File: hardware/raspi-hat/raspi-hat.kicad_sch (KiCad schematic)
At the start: 7 parts, among them J1 ATX-20, J2 Raspberry_Pi_4, U1 STSPIN32G4, Y1 Crystal_GND23_Small

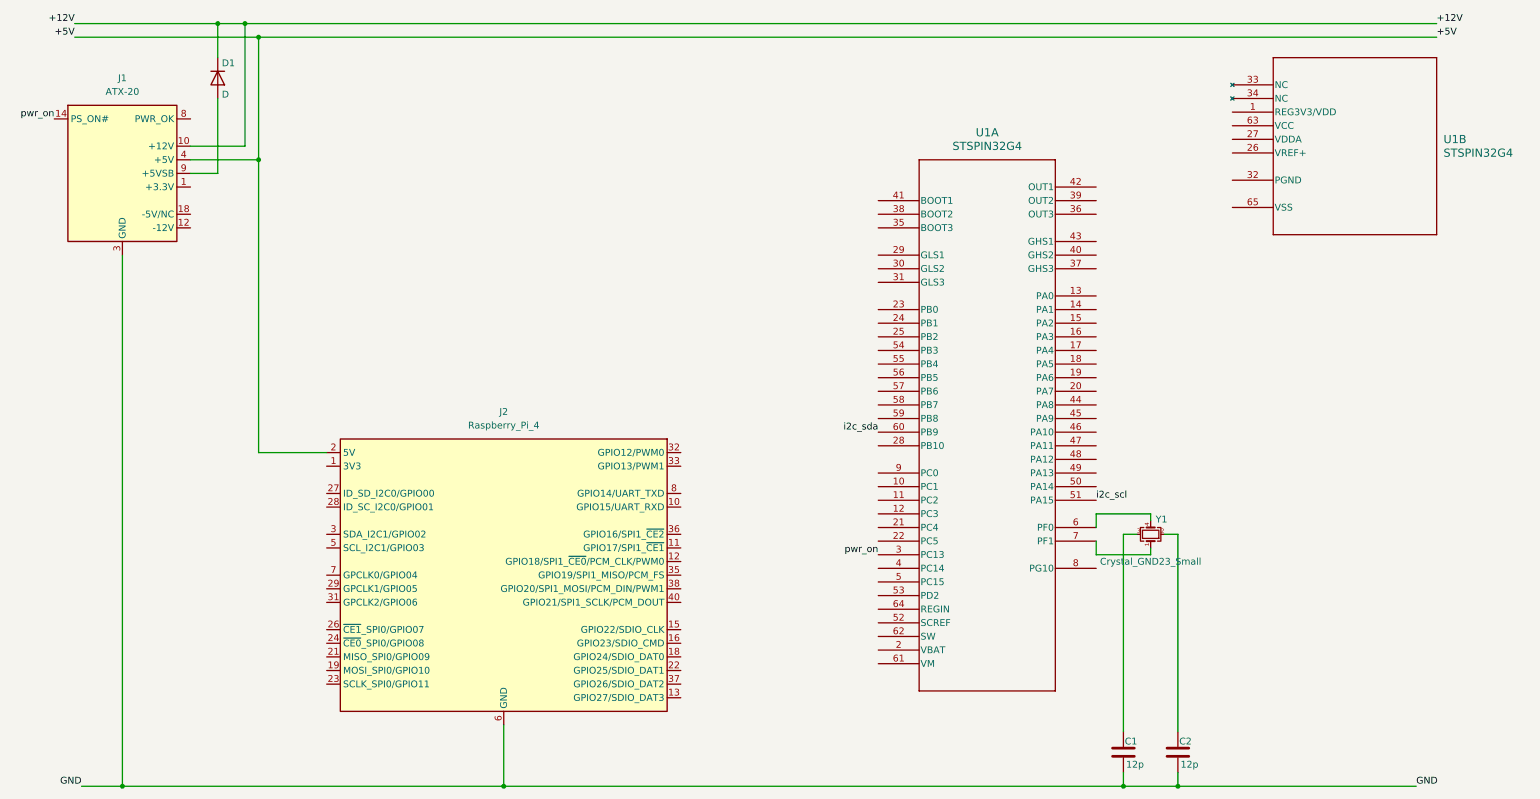
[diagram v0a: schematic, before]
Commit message: updated symbol of stsping4
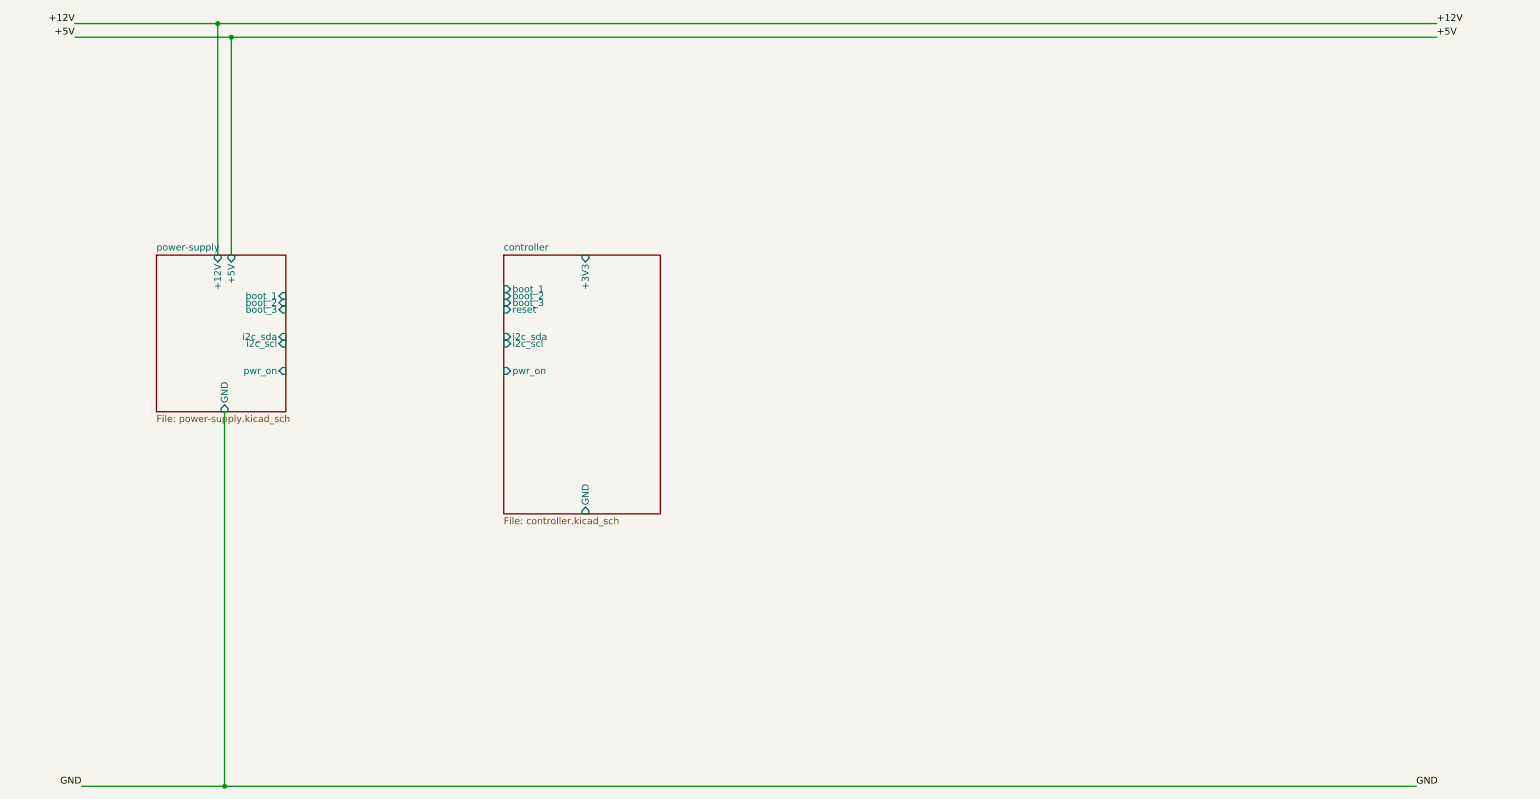
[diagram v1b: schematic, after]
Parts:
- removed C1, C2: 12p, Capacitor_SMD:C_0603_1608Metric, symbol Device:C
- removed D1: D, symbol Device:D
- removed J1: ATX-20, Connector_Molex:Molex_Mini-Fit_Jr_5569-20A2_2x10_P4.20mm_Horizontal, symbol Connector:ATX-20
- removed J2: Raspberry_Pi_4, symbol Connector:Raspberry_Pi_4
- removed U1: STSPIN32G4, QFN_IN32G4_STM, symbol stsping4:STSPIN32G4
- removed Y1: Crystal_GND23_Small, Crystal:Crystal_SMD_0603-4Pin_6.0x3.5mm, symbol Device:Crystal_GND23_Small
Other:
- added sheet controller (controller.kicad_sch)
- added sheet power-supply (power-supply.kicad_sch)

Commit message: - added some lines on hardwaer - added libmotor as dependency
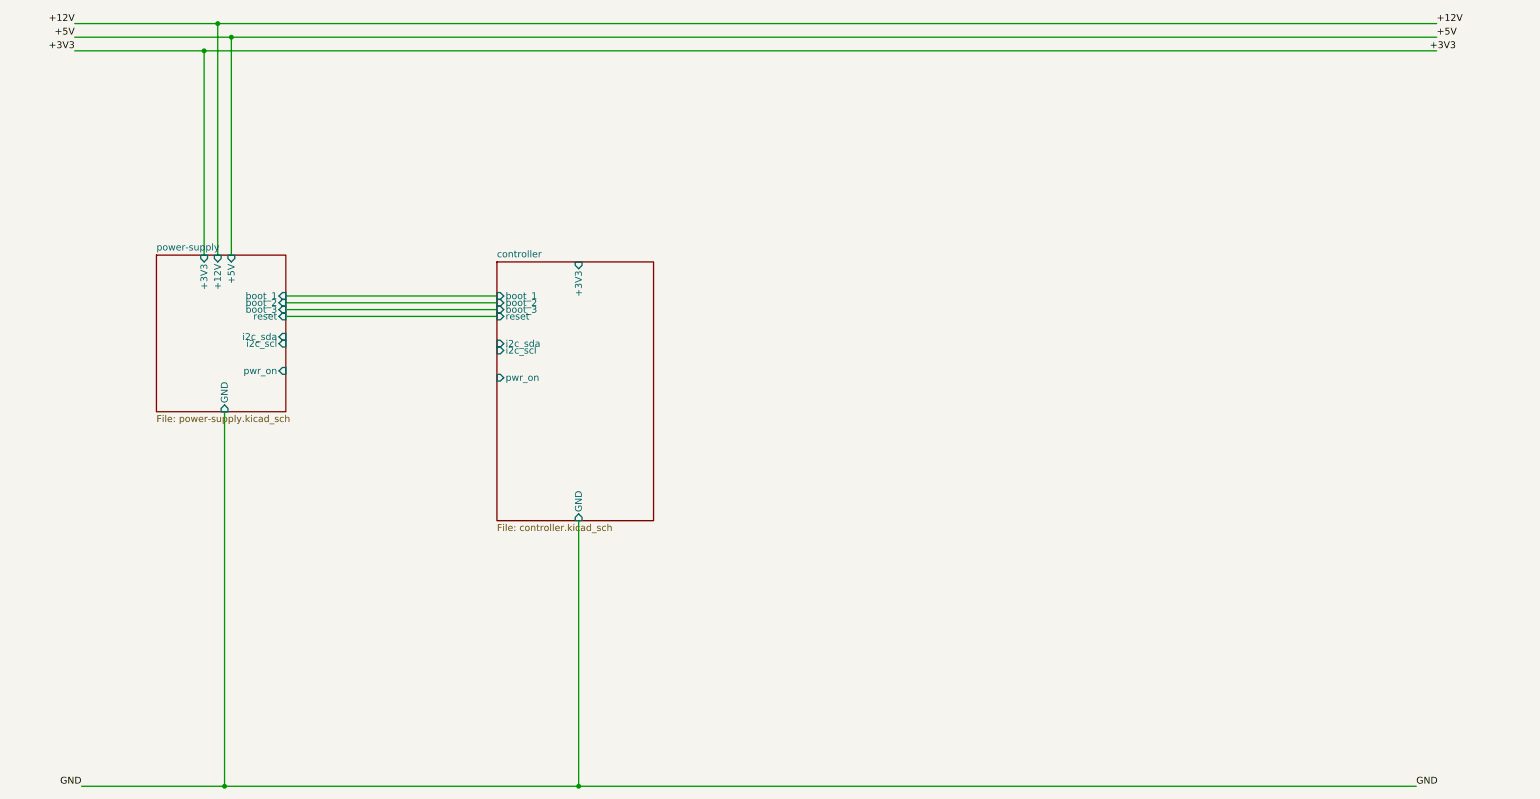
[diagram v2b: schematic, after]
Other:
- sheet power-supply ports: added +3V3, reset; removed none
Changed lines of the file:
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@@
+	)
+	(junction
+		(at 46.99 24.13)
+		(diameter 0)
+		(color 0 0 0 0)
 	)
 	(junction
@@
 		(color 0 0 0 0)
 	)
+	(junction
+		(at 116.84 161.29)
+		(diameter 0)
+		(color 0 0 0 0)
+	)
 	(wire
 		(pts
@@
 	(wire
 		(pts
+			(xy 46.99 62.23) (xy 46.99 24.13)
+		)
+		(stroke
+			(width 0)
+			(type default)
+		)
+	)
+	(wire
+		(pts
+			(xy 22.86 24.13) (xy 46.99 24.13)
+		)
+		(stroke
+			(width 0)
+			(type default)
+		)
+	)
+	(wire
+		(pts
 			(xy 22.86 19.05) (xy 49.53 19.05)
 		)
@@
 	(wire
 		(pts
+			(xy 62.23 71.12) (xy 101.6 71.12)
+		)
+		(stroke
+			(width 0)
+			(type default)
+		)
+	)
+	(wire
+		(pts
+			(xy 116.84 111.76) (xy 116.84 161.29)
+		)
+		(stroke
+			(width 0)
+			(type default)
+		)
+	)
+	(wire
+		(pts
 			(xy 52.07 21.59) (xy 52.07 62.23)
 		)
@@
 	(wire
 		(pts
+			(xy 46.99 24.13) (xy 276.86 24.13)
+		)
+		(stroke
+			(width 0)
+			(type default)
+		)
+	)
+	(wire
+		(pts
 			(xy 50.8 91.44) (xy 50.8 161.29)
 		)
@@
 	(wire
 		(pts
+			(xy 116.84 161.29) (xy 273.05 161.29)
+		)
+		(stroke
+			(width 0)
+			(type default)
+		)
+	)
+	(wire
+		(pts
 			(xy 52.07 21.59) (xy 276.86 21.59)
 		)
@@
 	(wire
 		(pts
-			(xy 50.8 161.29) (xy 273.05 161.29)
+			(xy 62.23 73.66) (xy 101.6 73.66)
+		)
+		(stroke
+			(width 0)
+			(type default)
+		)
+	)
+	(wire
+		(pts
+			(xy 62.23 72.39) (xy 101.6 72.39)
+		)
+		(stroke
+			(width 0)
+			(type default)
+		)
+	)
+	(wire
+		(pts
+			(xy 50.8 161.29) (xy 116.84 161.29)
 		)
 		(stroke
@@
 		(pts
 			(xy 22.86 21.59) (xy 52.07 21.59)
+		)
+		(stroke
+			(width 0)
+			(type default)
+		)
+	)
+	(wire
+		(pts
+			(xy 62.23 69.85) (xy 101.6 69.85)
 		)
 		(stroke
@@
 		)
 	)
+	(label "+3V3"
+		(at 275.59 24.13 0)
+		(effects
+			(font
+				(size 1.27 1.27)
+			)
+			(justify left bottom)
+		)
+	)
 	(label "+12V"
 		(at 276.86 19.05 0)
@@
 	(label "GND"
 		(at 24.13 161.29 180)
+		(effects
+			(font
+				(size 1.27 1.27)
+			)
+			(justify right bottom)
+		)
+	)
+	(label "+3V3"
+		(at 22.86 24.13 180)
 		(effects
 			(font
@@
 			)
 		)
+		(pin "reset" input
+			(at 62.23 73.66 0)
+			(effects
+				(font
+					(size 1.27 1.27)
+				)
+				(justify right)
+			)
+		)
+		(pin "+3V3" input
+			(at 46.99 62.23 90)
+			(effects
+				(font
+					(size 1.27 1.27)
+				)
+				(justify right)
+			)
+		)
 		(instances
 			(project "raspi-hat"
@@
 	)
 	(sheet
-		(at 102.87 62.23)
+		(at 101.6 63.5)
 		(size 29.21 48.26)
 		(exclude_from_sim no)
@@
 		)
 		(property "Sheetname" "controller"
-			(at 102.87 61.5184 0)
+			(at 101.6 62.7884 0)
 			(effects
 				(font
@@
 		)
 		(property "Sheetfile" "controller.kicad_sch"
-			(at 102.87 111.0746 0)
+			(at 101.6 112.3446 0)
 			(effects
 				(font
@@
 		)
 		(pin "+3V3" input
-			(at 118.11 62.23 90)
+			(at 116.84 63.5 90)
 			(effects
 				(font
@@
 		)
 		(pin "boot_1" input
-			(at 102.87 68.58 180)
+			(at 101.6 69.85 180)
 			(effects
 				(font
@@
 		)
 		(pin "boot_2" input
-			(at 102.87 69.85 180)
+			(at 101.6 71.12 180)
 			(effects
 				(font
@@
 		)
 		(pin "boot_3" input
-			(at 102.87 71.12 180)
+			(at 101.6 72.39 180)
 			(effects
 				(font
@@
 		)
 		(pin "GND" input
-			(at 118.11 110.49 270)
+			(at 116.84 111.76 270)
 			(effects
 				(font
@@
 		)
 		(pin "i2c_scl" input
-			(at 102.87 78.74 180)
+			(at 101.6 80.01 180)
 			(effects
 				(font
@@
 		)
 		(pin "i2c_sda" input
-			(at 102.87 77.47 180)
+			(at 101.6 78.74 180)
 			(effects
 				(font
@@
 		)
 		(pin "pwr_on" input
-			(at 102.87 83.82 180)
+			(at 101.6 85.09 180)
 			(effects
 				(font
@@
 		)
 		(pin "reset" input
-			(at 102.87 72.39 180)
-			(effects
-				(font
+			(at 101.6 73.66 180)
+			(effects
+				(font

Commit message: updatd ioc
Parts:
- added J2: Conn_01x03_Pin, symbol Connector:Conn_01x03_Pin
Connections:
- new net controller/phase_u: J2.1 (Pin_1)
- new net controller/phase_v: J2.2 (Pin_2)
- new net controller/phase_w: J2.3 (Pin_3)
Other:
- sheet controller ports: added +12V, boot, phase_u, phase_v, phase_w, uart_rx, uart_tx; removed boot_1, boot_2, boot_3, i2c_scl, i2c_sda, pwr_on
- sheet power-supply ports: added boot, uart_rx, uart_tx; removed boot_1, boot_2, boot_3

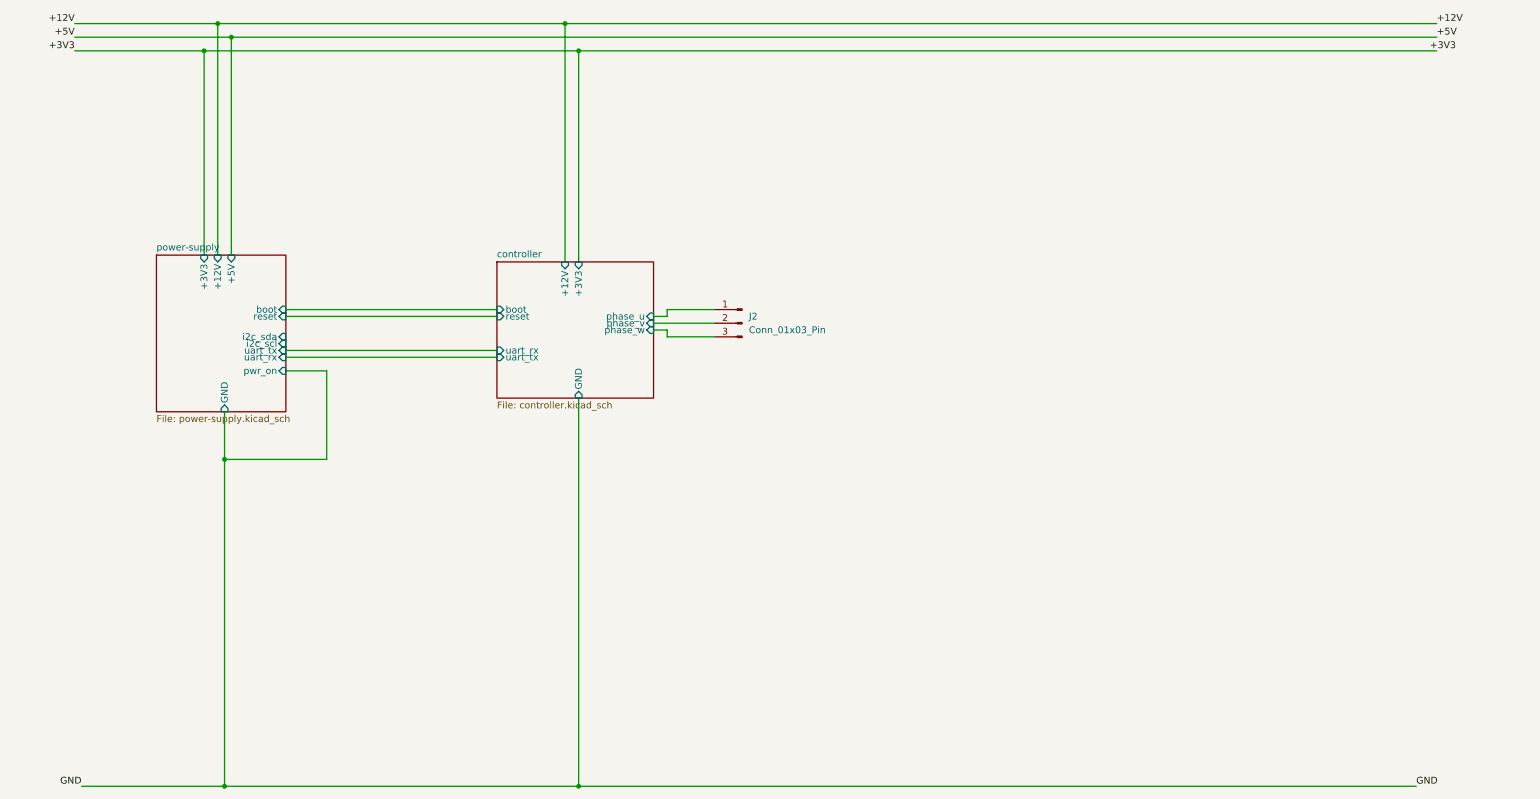
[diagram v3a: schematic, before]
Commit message: added more parts
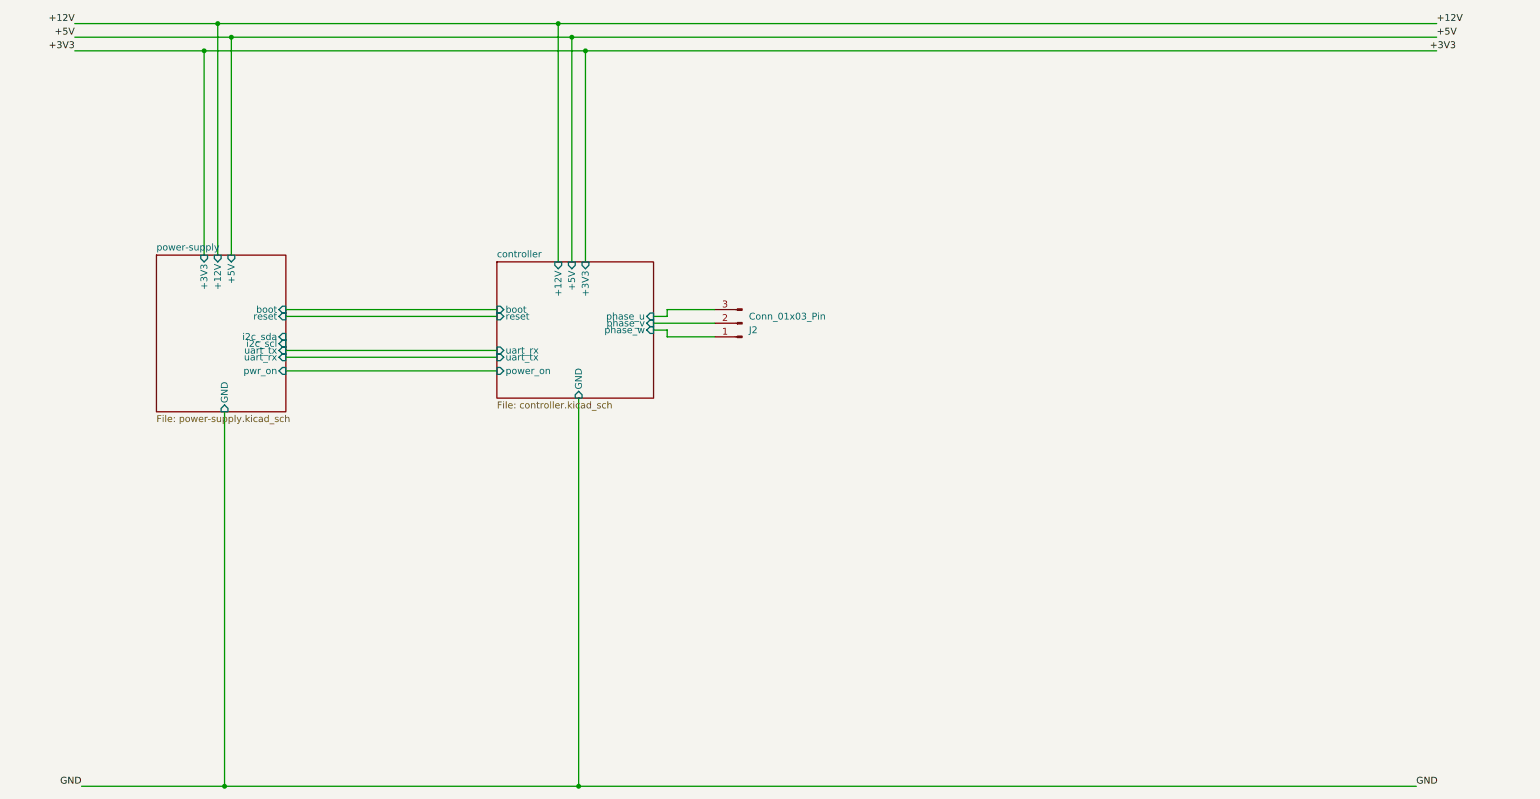
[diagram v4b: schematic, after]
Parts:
- J2: footprint (none) -> Connector_Phoenix_MSTB:PhoenixContact_MSTBA_2,5_3-G_1x03_P5.00mm_Horizontal
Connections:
- net controller/phase_u: now also J2.3 (Pin_3); no longer J2.1 (Pin_1)
- net controller/phase_w: now also J2.1 (Pin_1); no longer J2.3 (Pin_3)
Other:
- sheet controller ports: added +5V, power_on; removed none
- moved on the sheet: J2
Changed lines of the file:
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@@
-	)
-	(junction
-		(at 50.8 100.33)
-		(diameter 0)
-		(color 0 0 0 0)
-	)
-	(junction
-		(at 116.84 24.13)
-		(diameter 0)
-		(color 0 0 0 0)
 	)
 	(junction
@@
 	)
 	(junction
-		(at 114.3 19.05)
+		(at 118.11 24.13)
+		(diameter 0)
+		(color 0 0 0 0)
+	)
+	(junction
+		(at 113.03 19.05)
 		(diameter 0)
 		(color 0 0 0 0)
@@
 		(color 0 0 0 0)
 	)
+	(junction
+		(at 115.57 21.59)
+		(diameter 0)
+		(color 0 0 0 0)
+	)
+	(wire
+		(pts
+			(xy 113.03 19.05) (xy 276.86 19.05)
+		)
+		(stroke
+			(width 0)
+			(type default)
+		)
+	)
 	(wire
 		(pts
@@
 	(wire
 		(pts
-			(xy 116.84 24.13) (xy 276.86 24.13)
-		)
-		(stroke
-			(width 0)
-			(type default)
-		)
-	)
-	(wire
-		(pts
 			(xy 52.07 21.59) (xy 52.07 62.23)
 		)
@@
 	(wire
 		(pts
-			(xy 114.3 19.05) (xy 276.86 19.05)
-		)
-		(stroke
-			(width 0)
-			(type default)
-		)
-	)
-	(wire
-		(pts
-			(xy 46.99 24.13) (xy 116.84 24.13)
+			(xy 115.57 21.59) (xy 276.86 21.59)
+		)
+		(stroke
+			(width 0)
+			(type default)
+		)
+	)
+	(wire
+		(pts
+			(xy 46.99 24.13) (xy 118.11 24.13)
 		)
 		(stroke
@@
 	(wire
 		(pts
-			(xy 116.84 24.13) (xy 116.84 63.5)
+			(xy 118.11 24.13) (xy 118.11 63.5)
 		)
 		(stroke
@@
 	(wire
 		(pts
-			(xy 69.85 83.82) (xy 69.85 100.33)
-		)
-		(stroke
-			(width 0)
-			(type default)
-		)
-	)
-	(wire
-		(pts
-			(xy 50.8 91.44) (xy 50.8 100.33)
-		)
-		(stroke
-			(width 0)
-			(type default)
-		)
-	)
-	(wire
-		(pts
-			(xy 69.85 100.33) (xy 50.8 100.33)
+			(xy 50.8 91.44) (xy 50.8 161.29)
 		)
 		(stroke
@@
 	(wire
 		(pts
-			(xy 52.07 21.59) (xy 276.86 21.59)
+			(xy 52.07 21.59) (xy 115.57 21.59)
 		)
 		(stroke
@@
 	(wire
 		(pts
-			(xy 49.53 19.05) (xy 114.3 19.05)
+			(xy 49.53 19.05) (xy 113.03 19.05)
+		)
+		(stroke
+			(width 0)
+			(type default)
+		)
+	)
+	(wire
+		(pts
+			(xy 118.11 24.13) (xy 276.86 24.13)
 		)
 		(stroke
@@
 	(wire
 		(pts
+			(xy 115.57 21.59) (xy 115.57 63.5)
+		)
+		(stroke
+			(width 0)
+			(type default)
+		)
+	)
+	(wire
+		(pts
 			(xy 49.53 19.05) (xy 49.53 62.23)
 		)
@@
 	(wire
 		(pts
-			(xy 114.3 19.05) (xy 114.3 63.5)
+			(xy 113.03 19.05) (xy 113.03 63.5)
 		)
 		(stroke
@@
 	(wire
 		(pts
-			(xy 50.8 100.33) (xy 50.8 161.29)
-		)
-		(stroke
-			(width 0)
-			(type default)
-		)
-	)
-	(wire
-		(pts
-			(xy 62.23 83.82) (xy 69.85 83.82)
+			(xy 62.23 83.82) (xy 101.6 83.82)
 		)
 		(stroke
@@
 	(symbol
 		(lib_id "Connector:Conn_01x03_Pin")
-		(at 147.32 74.93 0)
-		(mirror y)
+		(at 147.32 74.93 180)
 		(unit 1)
 		(exclude_from_sim no)
@@
 		(on_board yes)
 		(dnp no)
-		(fields_autoplaced yes)
 		(property "Reference" "J2"
-			(at 148.59 73.6599 0)
+			(at 148.59 76.2001 0)
 			(effects
 				(font
@@
 		)
 		(property "Value" "Conn_01x03_Pin"
-			(at 148.59 76.1999 0)
-			(effects
-				(font
-					(size 1.27 1.27)
-				)
-				(justify right)
-			)
-		)
-		(property "Footprint" ""
+			(at 148.59 73.6601 0)
+			(effects
+				(font
+					(size 1.27 1.27)
+				)
+				(justify right)
+			)
+		)
+		(property "Footprint" "Connector_Phoenix_MSTB:PhoenixContact_MSTBA_2,5_3-G_1x03_P5.00mm_Horizontal"
 			(at 147.32 74.93 0)
 			(effects
@@
 		)
 		(pin "+3V3" input
-			(at 116.84 63.5 90)
+			(at 118.11 63.5 90)
 			(effects
 				(font
@@
 		)
 		(pin "+12V" input
-			(at 114.3 63.5 90)
+			(at 113.03 63.5 90)
 			(effects
 				(font
@@
 			)
 		)
+		(pin "+5V" input
+			(at 115.57 63.5 90)
+			(effects
+				(font
+					(size 1.27 1.27)
+				)
+				(justify right)
+			)
+		)
+		(pin "power_on" input
+			(at 101.6 83.82 180)
+			(effects
+				(font
+					(size 1.27 1.27)
+				)
+				(justify left)
+			)
+		)
